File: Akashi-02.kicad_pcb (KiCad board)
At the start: 2 copper layers, 52.7 x 80.6 mm, 26 parts, among them CN10 Conn_02x17_Odd_Even, CN7 Conn_02x10_Odd_Even, CN8 Conn_02x08_Odd_Even, CN9 Conn_02x15_Odd_Even, U1 UMB-SSM2603B, U2 UMB-ADAU1361A

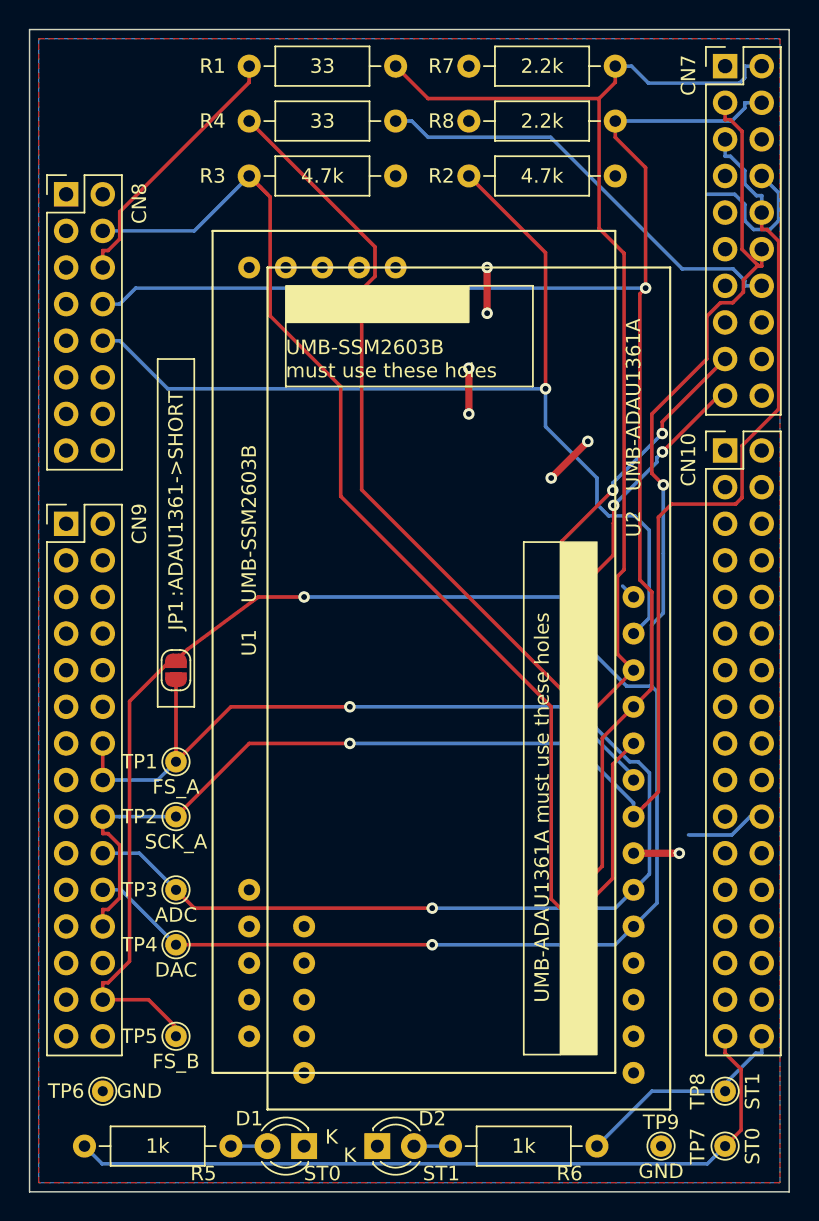
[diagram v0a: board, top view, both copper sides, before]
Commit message: Added README.md
Prepare to be public, after the submittion of gerber to fab.
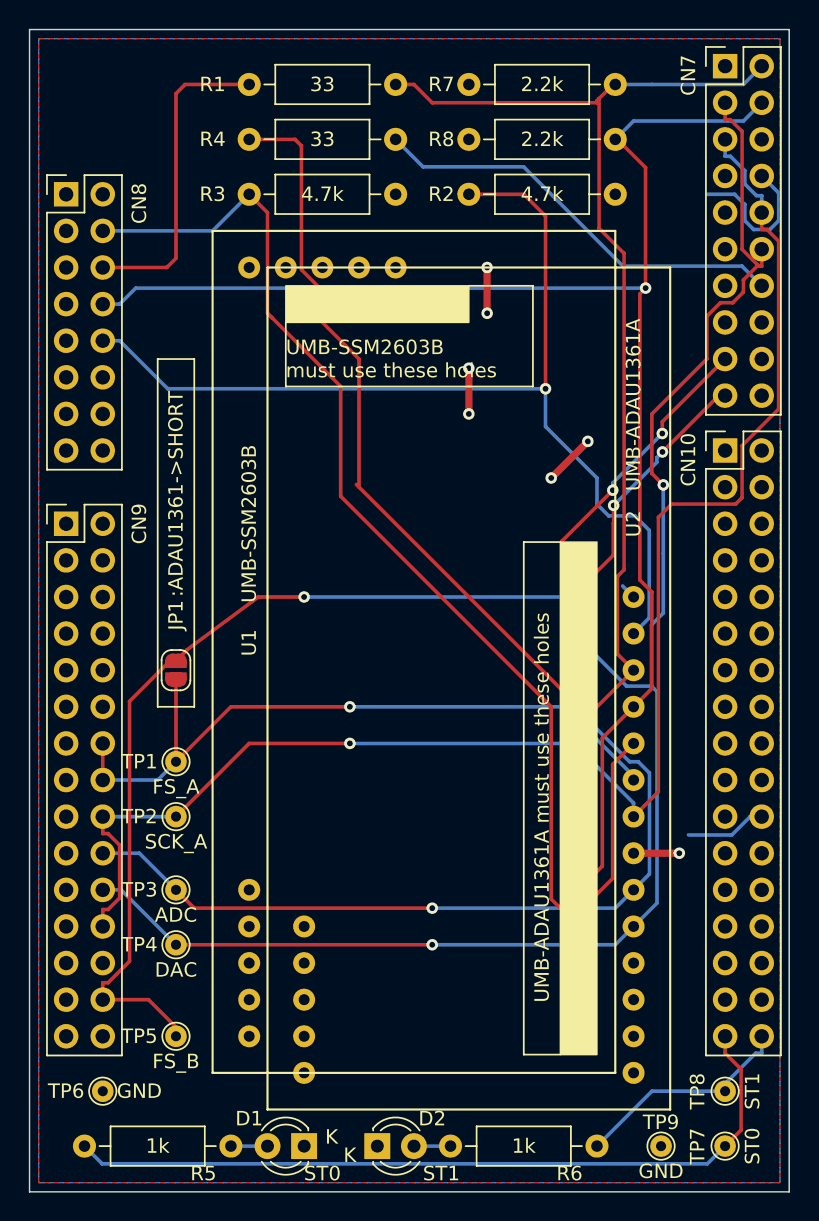
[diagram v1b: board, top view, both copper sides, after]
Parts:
- moved R2 1.27 mm to (134.6, 66.0)
- moved R3 1.27 mm to (119.4, 66.0)
- moved R1 1.27 mm to (129.5, 58.4)
- moved R7 1.27 mm to (134.6, 58.4)
- moved R4 1.27 mm to (119.4, 62.2)
- moved R8 1.27 mm to (134.6, 62.2)
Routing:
- net /SPI3_SCK: track 18.4 -> 22.1 mm
- net /SPI_SS: track 89.4 -> 85.9 mm
- net /I2C1_SCL: track 84.7 -> 82.4 mm
- net /SPI3_MOSI: track 70.6 -> 71.5 mm
- net /I2C1_SDA: track 105.9 -> 105.0 mm
- net /I2S1_SD: track 30.3 -> 29.6 mm
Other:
- board text added: "Akashi-02 CODEC Test board for Nucleo 144 (C) Seiichi Horie 2019 https://github.com/suikan4github/Akashi-02"
- board text removed: "Kiritsubo 2 (C) Seiichi Horie 2019"

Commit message: Change drill size of the test point
Issue : Test pin hole is too small #1
https://github.com/suikan4github/Akashi-02/issues/1
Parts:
- TP1, TP2, TP3, TP4, TP5, TP6, TP7, TP8, TP9: footprint TestPoint:TestPoint_THTPad_D1.5mm_Drill0.7mm -> TestPoint:TestPoint_THTPad_D2.0mm_Drill1.0mm

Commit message: Change size of the COPYRIGHT
Issue : Copy right is too small #2
https://github.com/suikan4github/Akashi-02/issues/2
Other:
- board text added: "Akashi-02 v1.0.1 CODEC Test board for Nucleo 144 (C) Seiichi Horie 2019 https://github.com/suikan4github/Akashi-02"
- board text removed: "Akashi-02 CODEC Test board for Nucleo 144 (C) Seiichi Horie 2019 https://github.com/suikan4github/Akashi-02"
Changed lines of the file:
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@@
     (effects (font (size 1 1) (thickness 0.15)) (justify left))
   )
-  (gr_text "Akashi-02\nCODEC Test board for Nucleo 144 \n(C) Seiichi Horie 2019\nhttps://github.com/suikan4github/Akashi-02" (at 120.015 109.855 -90) (layer B.SilkS)
-    (effects (font (size 1 1) (thickness 0.15)) (justify left mirror))
+  (gr_text "Akashi-02 v1.0.1\nCODEC Test board for Nucleo 144 \n(C) Seiichi Horie 2019\nhttps://github.com/suikan4github/Akashi-02" (at 130.175 128.27 -90) (layer B.SilkS)
+    (effects (font (size 1.5 1.5) (thickness 0.15)) (justify left mirror))
   )
   (segment (start 144.6082 86.5721) (end 144.6082 86.0698) (width 0.25) (layer B.Cu) (net 1))
